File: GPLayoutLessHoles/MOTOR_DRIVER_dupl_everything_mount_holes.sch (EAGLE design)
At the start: 194 parts, among them T1 2N2222, T2 2N2222, T3 2N2222, T4 2N2222, U1 ATMEGA328P_TQFP, U7 ATMEGA328P_TQFP, Y1 16MHz, Y2 16MHz

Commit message: added more mounting holes and headers, renamed switches. ordered this 3/20
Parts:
- added H10, H11, H12, H13, H14, H15, H16, H9: MOUNT-HOLE3.3, holes:MOUNT-HOLE3.3
- added SV19, SV20: (no value), con-lsta:FE04-1
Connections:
- new net THERM1: LED1.THERMAL
- new net THERM1_DUP: LED3.THERMAL
- new net THERM2: LED2.THERMAL
- new net THERM2_DUP: LED4.THERMAL
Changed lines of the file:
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@@
 <part name="H7" library="holes" deviceset="MOUNT-HOLE" device="3.6"/>
 <part name="H8" library="holes" deviceset="MOUNT-HOLE" device="3.6"/>
+<part name="SV19" library="con-lsta" deviceset="FE04-1" device=""/>
+<part name="SV20" library="con-lsta" deviceset="FE04-1" device=""/>
+<part name="H9" library="holes" deviceset="MOUNT-HOLE" device="3.3"/>
+<part name="H10" library="holes" deviceset="MOUNT-HOLE" device="3.3"/>
+<part name="H11" library="holes" deviceset="MOUNT-HOLE" device="3.3"/>
+<part name="H12" library="holes" deviceset="MOUNT-HOLE" device="3.3"/>
+<part name="H13" library="holes" deviceset="MOUNT-HOLE" device="3.3"/>
+<part name="H14" library="holes" deviceset="MOUNT-HOLE" device="3.3"/>
+<part name="H15" library="holes" deviceset="MOUNT-HOLE" device="3.3"/>
+<part name="H16" library="holes" deviceset="MOUNT-HOLE" device="3.3"/>
 </parts>
 <sheets>
@@
 <instance part="SV6" gate="G$1" x="96.52" y="205.74"/>
 <instance part="SV5" gate="G$1" x="48.26" y="213.36"/>
+<instance part="SV19" gate="G$1" x="233.68" y="203.2"/>
 </instances>
 <busses>
@@
 <instance part="R16" gate="G$1" x="88.9" y="195.58" rot="R90"/>
 <instance part="C8" gate="G$1" x="198.12" y="210.82"/>
+<instance part="H9" gate="G$1" x="226.06" y="233.68"/>
+<instance part="H10" gate="G$1" x="238.76" y="233.68"/>
+<instance part="H11" gate="G$1" x="251.46" y="233.68"/>
+<instance part="H12" gate="G$1" x="261.62" y="233.68"/>
 </instances>
 <busses>
@@
 </segment>
 </net>
+<net name="THERM1" class="0">
+<segment>
+<pinref part="LED1" gate="G$1" pin="THERMAL"/>
+<wire x1="254" y1="218.44" x2="248.92" y2="218.44" width="0.1524" layer="91"/>
+<label x="248.92" y="218.44" size="1.778" layer="95"/>
+</segment>
+</net>
+<net name="THERM2" class="0">
+<segment>
+<pinref part="LED2" gate="G$1" pin="THERMAL"/>
+<wire x1="309.88" y1="215.9" x2="307.34" y2="215.9" width="0.1524" layer="91"/>
+<label x="307.34" y="215.9" size="1.778" layer="95"/>
+</segment>
+</net>
 </nets>
 </sheet>
@@
 <instance part="SV17" gate="G$1" x="96.52" y="205.74"/>
 <instance part="SV18" gate="G$1" x="48.26" y="213.36"/>
+<instance part="SV20" gate="G$1" x="233.68" y="200.66"/>
 </instances>
 <busses>
@@
 <instance part="R34" gate="G$1" x="88.9" y="195.58" rot="R90"/>
 <instance part="C24" gate="G$1" x="198.12" y="210.82"/>
+<instance part="H13" gate="G$1" x="233.68" y="241.3"/>
+<instance part="H14" gate="G$1" x="254" y="241.3"/>
+<instance part="H15" gate="G$1" x="271.78" y="241.3"/>
+<instance part="H16" gate="G$1" x="289.56" y="241.3"/>
 </instances>
 <busses>
@@
 </segment>
 </net>
+<net name="THERM1_DUP" class="0">
+<segment>
+<pinref part="LED3" gate="G$1" pin="THERMAL"/>
+<wire x1="254" y1="218.44" x2="248.92" y2="218.44" width="0.1524" layer="91"/>
+<label x="248.92" y="218.44" size="1.778" layer="95"/>
+</segment>
+</net>
+<net name="THERM2_DUP" class="0">
+<segment>
+<pinref part="LED4" gate="G$1" pin="THERMAL"/>
+<wire x1="309.88" y1="215.9" x2="307.34" y2="215.9" width="0.1524" layer="91"/>
+<label x="307.34" y="215.9" size="1.778" layer="95"/>
+</segment>
+</net>

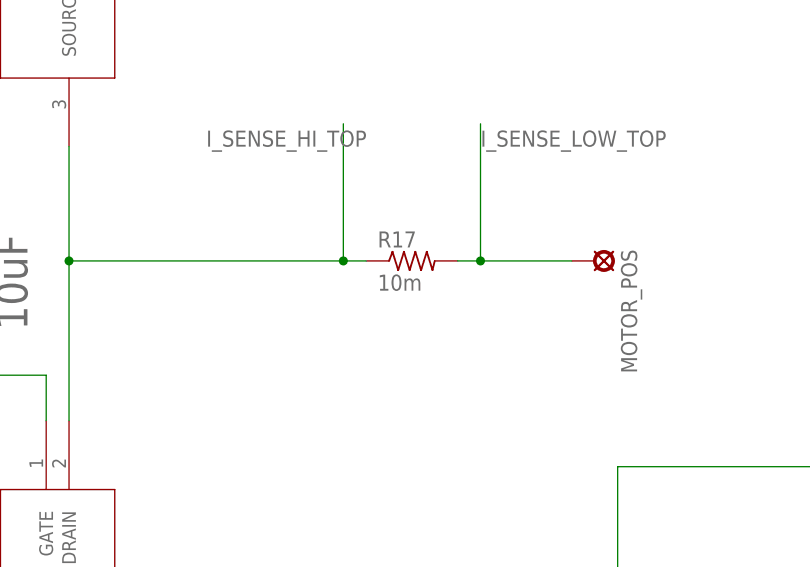
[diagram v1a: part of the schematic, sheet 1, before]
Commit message: some modified board and new driving code for single thread and half or full bridge
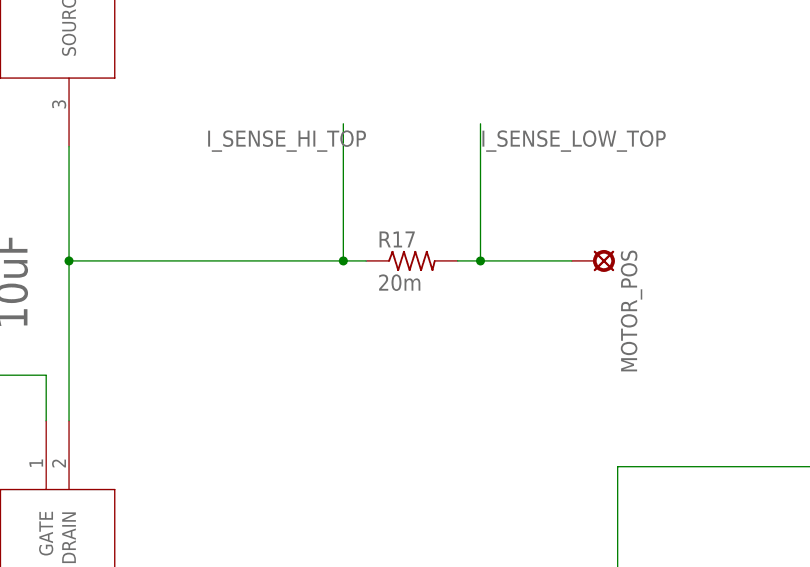
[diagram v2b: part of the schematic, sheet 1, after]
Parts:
- R17, R35: value 10m -> 20m
- R18, R36: value 10k -> 100k
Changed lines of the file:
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@@
 <part name="R16" library="resistor" deviceset="R-US_" device="R0603" value="10k"/>
 <part name="ATGPIO" library="con-lsta" deviceset="FE10-1" device=""/>
-<part name="R17" library="rcl" deviceset="R-US_" device="R2512" value="10m"/>
+<part name="R17" library="rcl" deviceset="R-US_" device="R2512" value="20m"/>
 <part name="I_SENSE_AMP" library="burr-brown" deviceset="INA138" device=""/>
-<part name="R18" library="rcl" deviceset="R-US_" device="R0603" value="10k"/>
+<part name="R18" library="rcl" deviceset="R-US_" device="R0603" value="100k"/>
 <part name="C7" library="resistor" deviceset="C-US" device="C0603"/>
 <part name="REC" library="con-lsta" deviceset="FE06-1" device=""/>
@@
 <part name="R34" library="resistor" deviceset="R-US_" device="R0603" value="10k"/>
 <part name="ATGPIO1" library="con-lsta" deviceset="FE10-1" device=""/>
-<part name="R35" library="rcl" deviceset="R-US_" device="R2512" value="10m"/>
+<part name="R35" library="rcl" deviceset="R-US_" device="R2512" value="20m"/>
 <part name="I_SENSE_AMP1" library="burr-brown" deviceset="INA138" device=""/>
-<part name="R36" library="rcl" deviceset="R-US_" device="R0603" value="10k"/>
+<part name="R36" library="rcl" deviceset="R-US_" device="R0603" value="100k"/>
 <part name="C23" library="resistor" deviceset="C-US" device="C0603"/>
 <part name="REC1" library="con-lsta" deviceset="FE06-1" device=""/>
